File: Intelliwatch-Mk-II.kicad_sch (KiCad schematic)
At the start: 74 parts, among them J1 Voltmeter Probes, J2 DC Power Input, J3 USB_C_Receptacle_USB2.0_16P, J4 Flashlight Terminals, J5 CONN LCD 1.8 TFT SPI, J6 Conn 7S-4D HW-069 I2C, Q1 NDS331N, SW1 PWR SPST, SW2 EN Button, SW3 LCD LED SPST, SW4 Cherry MX Keyswitch, SW5 Cherry MX Keyswitch, SW6 Cherry MX Keyswitch, SW7 Cherry MX Keyswitch, SW8 PROG Button, U1 SN74HC02N, U2 MCP3421A0T-ECH, U3 74AHC1G04GW_125, U4 74AHC1G04GW_125, U5 LM7805, U6 CH340C, U7 SY8120IABC, U8 QMC5883L, U9 ESP32-WROOM-32UE

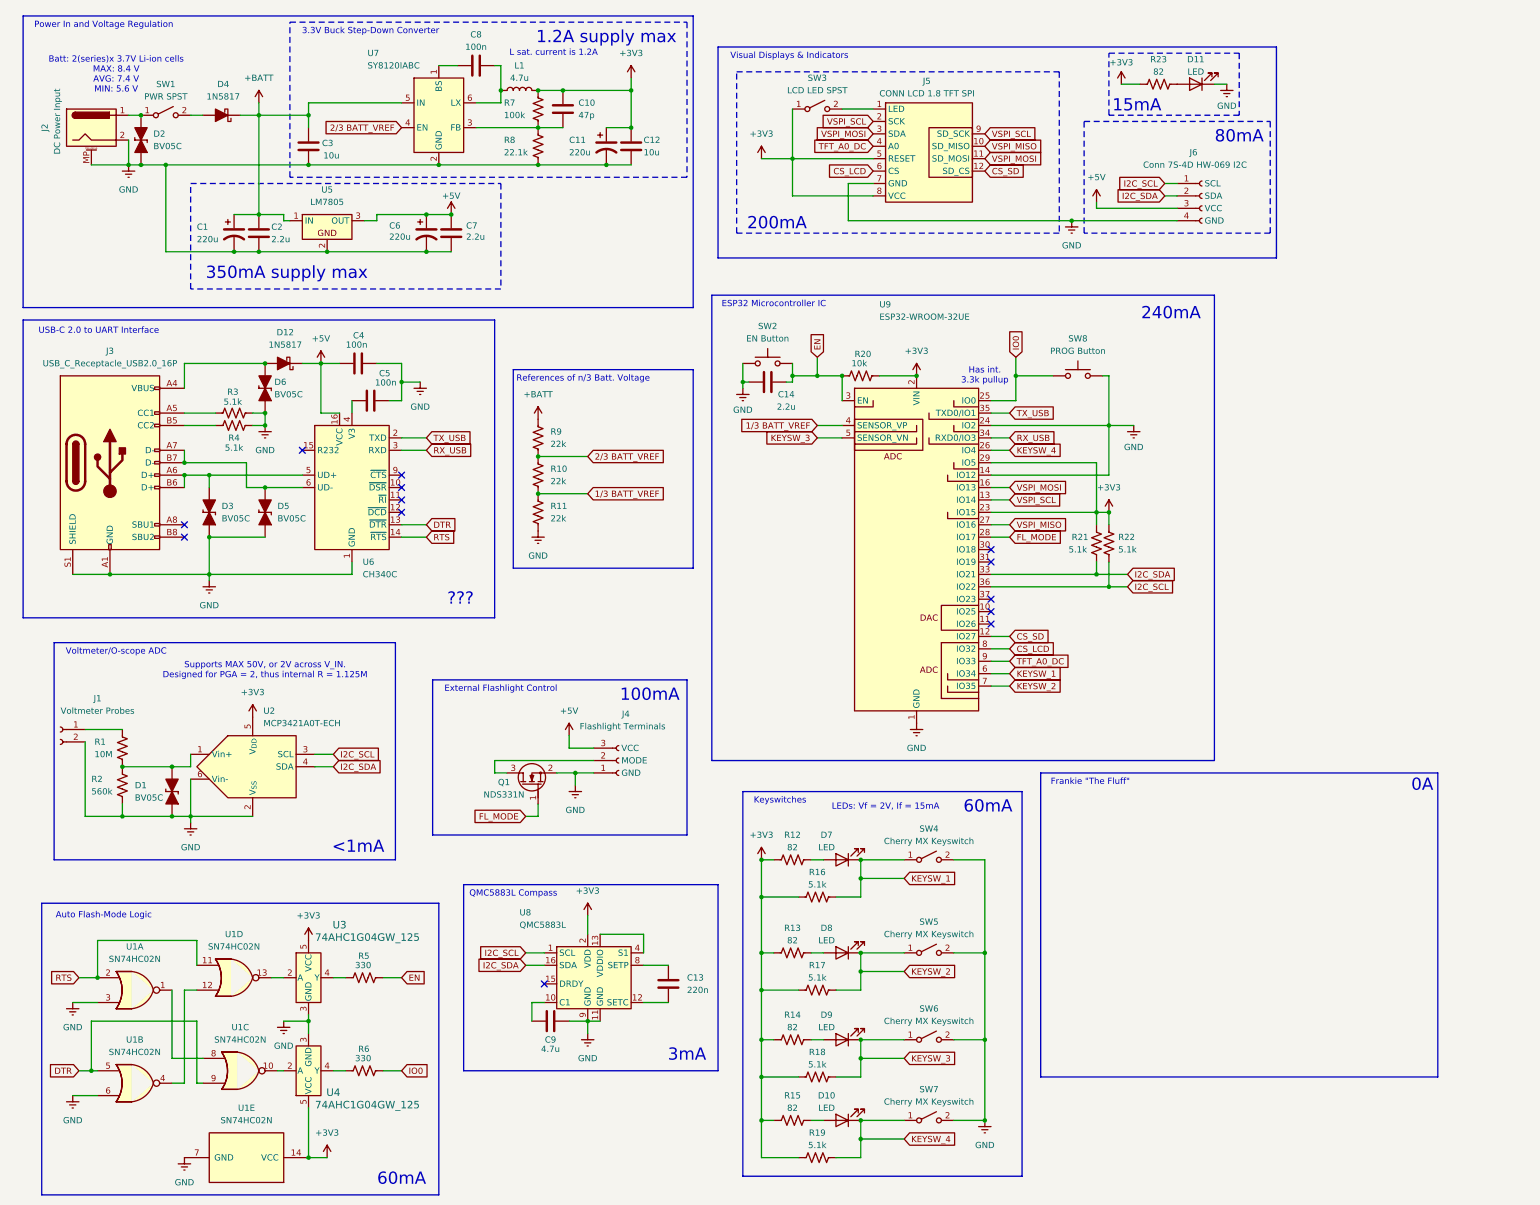
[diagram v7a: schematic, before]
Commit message: WIP TODO TFT LCD footprint. ADDED remaining LCSC part numbers. ADDED all basic setup specs and design rules for PCB. TODO is to arrange then route PCB, adding necessary 2.7mm diameter bolt holes.
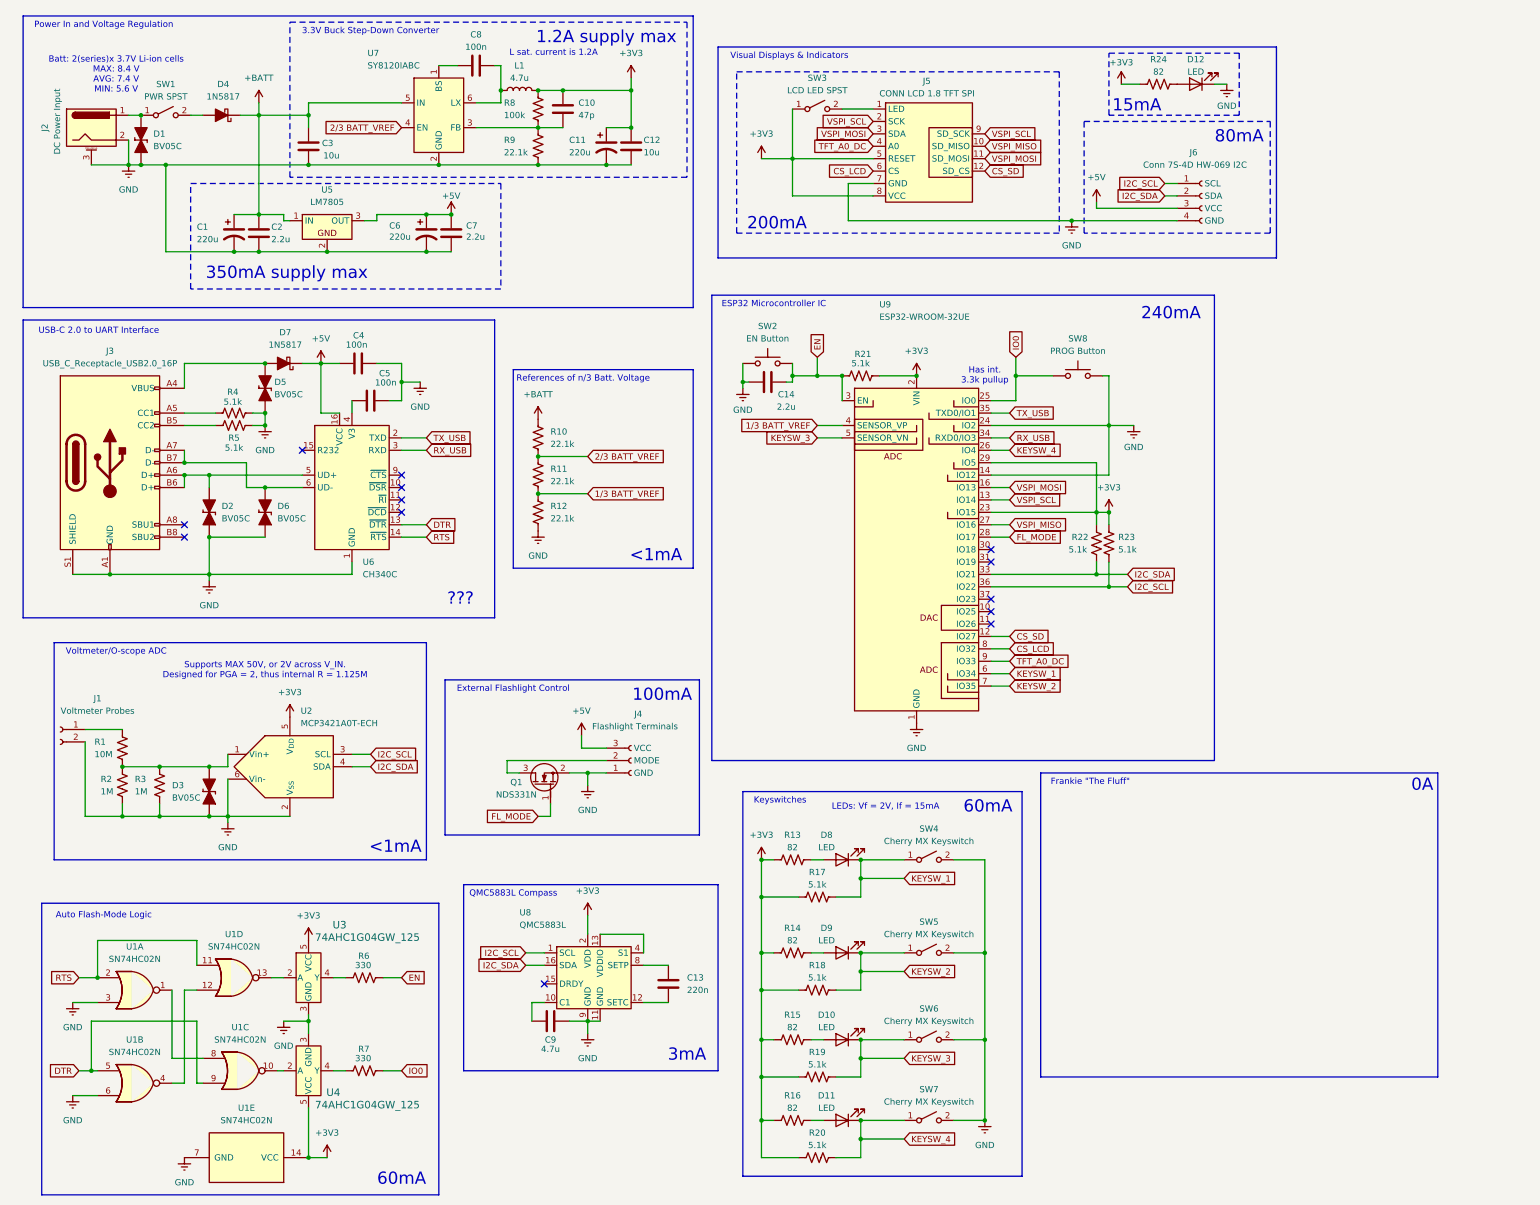
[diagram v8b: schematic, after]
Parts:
- added R3: 1M, ZCustomFootprints:Fav Res Axial 10.16mm, symbol Device:R_US
- C1, C11, C6: footprint (none) -> PCM_Capacitor_THT_US_AKL:CP_Radial_D6.3mm_P2.50mm
- D10: renamed from D9; footprint LED_SMD:LED_0603_1608Metric -> PCM_LED_SMD_AKL:LED_0603_1608Metric
- D11: renamed from D10; footprint LED_SMD:LED_0603_1608Metric -> PCM_LED_SMD_AKL:LED_0603_1608Metric
- D12: renamed from D11; footprint LED_SMD:LED_0603_1608Metric -> PCM_LED_SMD_AKL:LED_0603_1608Metric
- D4: footprint (none) -> Diode_THT:D_A-405_P10.16mm_Horizontal
- D7: renamed from D12; footprint (none) -> Diode_THT:D_A-405_P10.16mm_Horizontal
- D8: renamed from D7; footprint LED_SMD:LED_0603_1608Metric -> PCM_LED_SMD_AKL:LED_0603_1608Metric
- D9: renamed from D8; footprint LED_SMD:LED_0603_1608Metric -> PCM_LED_SMD_AKL:LED_0603_1608Metric
- R1: footprint (none) -> ZCustomFootprints:Fav Res Axial 10.16mm
- R10: renamed from R9; value 22k -> 22.1k; footprint (none) -> PCM_Resistor_SMD_AKL:R_0603_1608Metric; LCSC Part # (none) -> C5382621
- R11: renamed from R10; value 22k -> 22.1k; footprint (none) -> PCM_Resistor_SMD_AKL:R_0603_1608Metric; LCSC Part # (none) -> C5382621
- R12: renamed from R11; value 22k -> 22.1k; footprint (none) -> PCM_Resistor_SMD_AKL:R_0603_1608Metric; LCSC Part # (none) -> C5382621
- R13: renamed from R12; footprint (none) -> PCM_Resistor_SMD_AKL:R_0603_1608Metric; LCSC Part # (none) -> C861575
- R14: renamed from R13; footprint (none) -> PCM_Resistor_SMD_AKL:R_0603_1608Metric; LCSC Part # (none) -> C861575
- R15: renamed from R14; footprint (none) -> PCM_Resistor_SMD_AKL:R_0603_1608Metric; LCSC Part # (none) -> C861575
- R16: renamed from R15; footprint (none) -> PCM_Resistor_SMD_AKL:R_0603_1608Metric; LCSC Part # (none) -> C861575
- R17: renamed from R16; footprint (none) -> PCM_Resistor_SMD_AKL:R_0603_1608Metric; LCSC Part # (none) -> C318133
- R18: renamed from R17; footprint (none) -> PCM_Resistor_SMD_AKL:R_0603_1608Metric; LCSC Part # (none) -> C318133
- R19: renamed from R18; footprint (none) -> PCM_Resistor_SMD_AKL:R_0603_1608Metric; LCSC Part # (none) -> C318133
- R2: value 560k -> 1M; footprint (none) -> ZCustomFootprints:Fav Res Axial 10.16mm; LCSC Part # (none) -> n/a
- R20: renamed from R19; footprint (none) -> PCM_Resistor_SMD_AKL:R_0603_1608Metric; LCSC Part # (none) -> C318133
- R21: renamed from R20; value 10k -> 5.1k; footprint (none) -> PCM_Resistor_SMD_AKL:R_0603_1608Metric; LCSC Part # (none) -> C318133
- R22: renamed from R21; footprint (none) -> PCM_Resistor_SMD_AKL:R_0603_1608Metric; LCSC Part # (none) -> C318133
- R23: renamed from R22; footprint (none) -> PCM_Resistor_SMD_AKL:R_0603_1608Metric; LCSC Part # (none) -> C318133
- R24: renamed from R23; footprint (none) -> PCM_Resistor_SMD_AKL:R_0603_1608Metric; LCSC Part # (none) -> C861575
- R4: renamed from R3; footprint (none) -> PCM_Resistor_SMD_AKL:R_0603_1608Metric; LCSC Part # (none) -> C318133
- R5: renamed from R4; footprint (none) -> PCM_Resistor_SMD_AKL:R_0603_1608Metric; LCSC Part # (none) -> C318133
- R6: renamed from R5; footprint (none) -> PCM_Resistor_SMD_AKL:R_0603_1608Metric; LCSC Part # (none) -> C384242
- R7: renamed from R6; footprint (none) -> PCM_Resistor_SMD_AKL:R_0603_1608Metric; LCSC Part # (none) -> C384242
- R8: renamed from R7; footprint (none) -> PCM_Resistor_SMD_AKL:R_0603_1608Metric; LCSC Part # (none) -> C25803
- R9: renamed from R8; footprint (none) -> PCM_Resistor_SMD_AKL:R_0603_1608Metric; LCSC Part # (none) -> C5382621
- renumbered D2 to D1, D3 to D2, D1 to D3, D6 to D5, D5 to D6
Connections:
- net GND: now also J2.3 (MountPin), R3.2; no longer J2.MP (MountPin)
- net at D3.1 (K), R1.1, R2.1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: now also R3.1
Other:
- moved on the sheet: D3, J4, Q1, U2
